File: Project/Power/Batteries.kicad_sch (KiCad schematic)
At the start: 12 parts, among them J1 Battery, J2 Battery, J3 Battery, J4 Battery, Q3 SQJ138ELP, Q4 SQJ138ELP, Q5 SQJ138ELP, Q6 SQJ138ELP, U3 NCV68061, U4 NCV68061, U5 NCV68061, U6 NCV68061

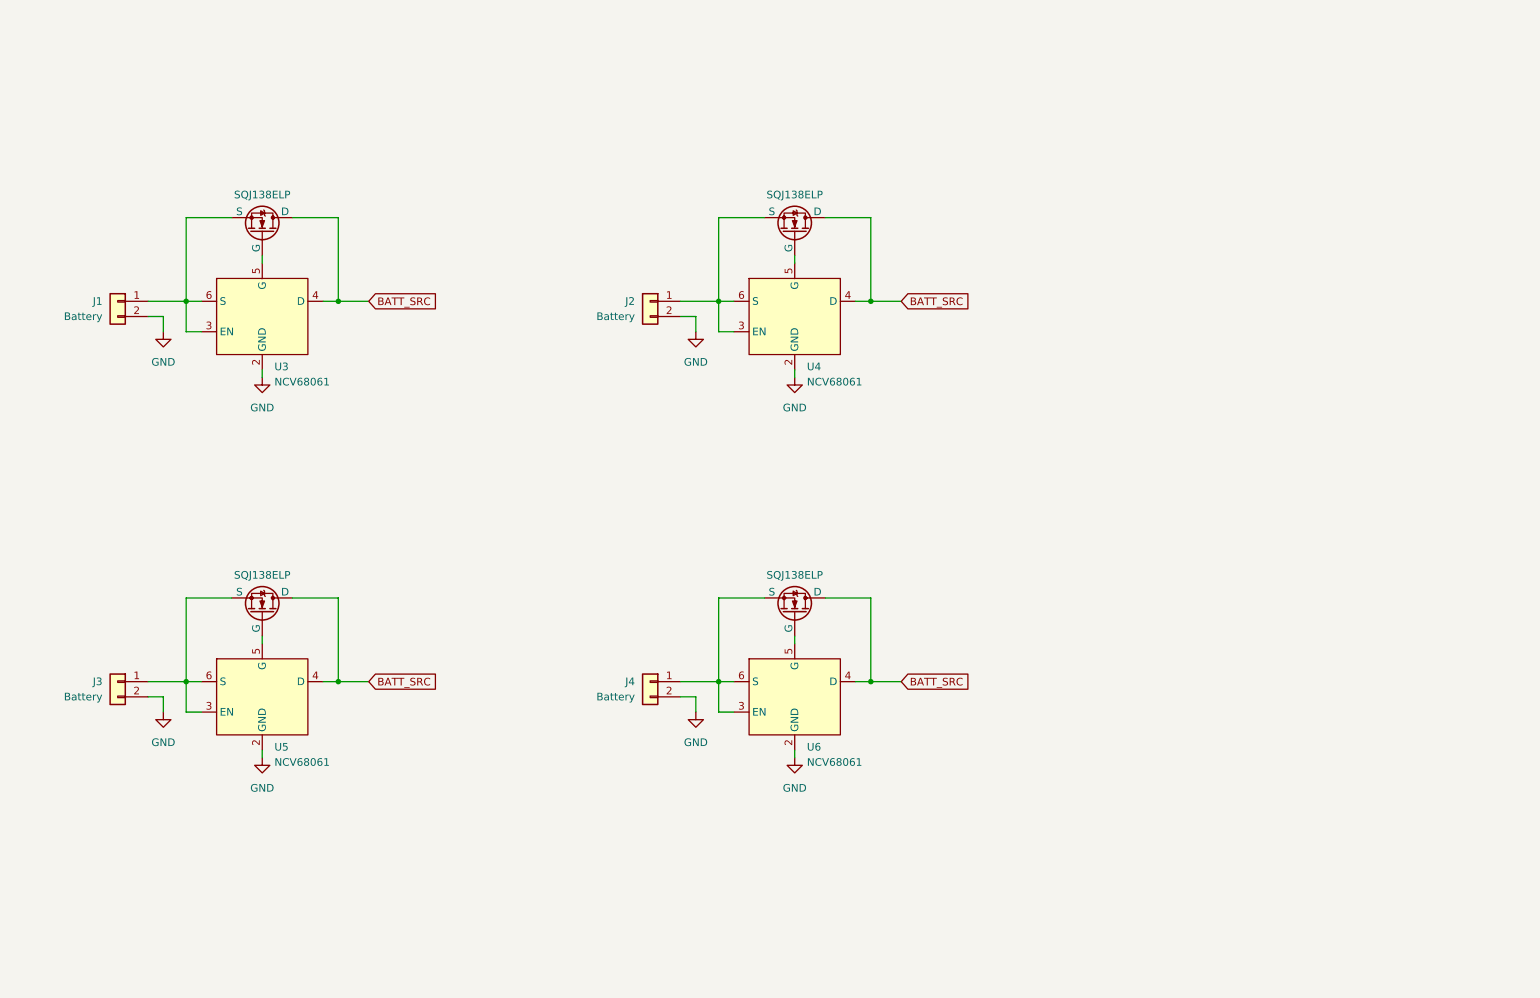
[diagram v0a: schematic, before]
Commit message: Add indicator LEDs to the batteries
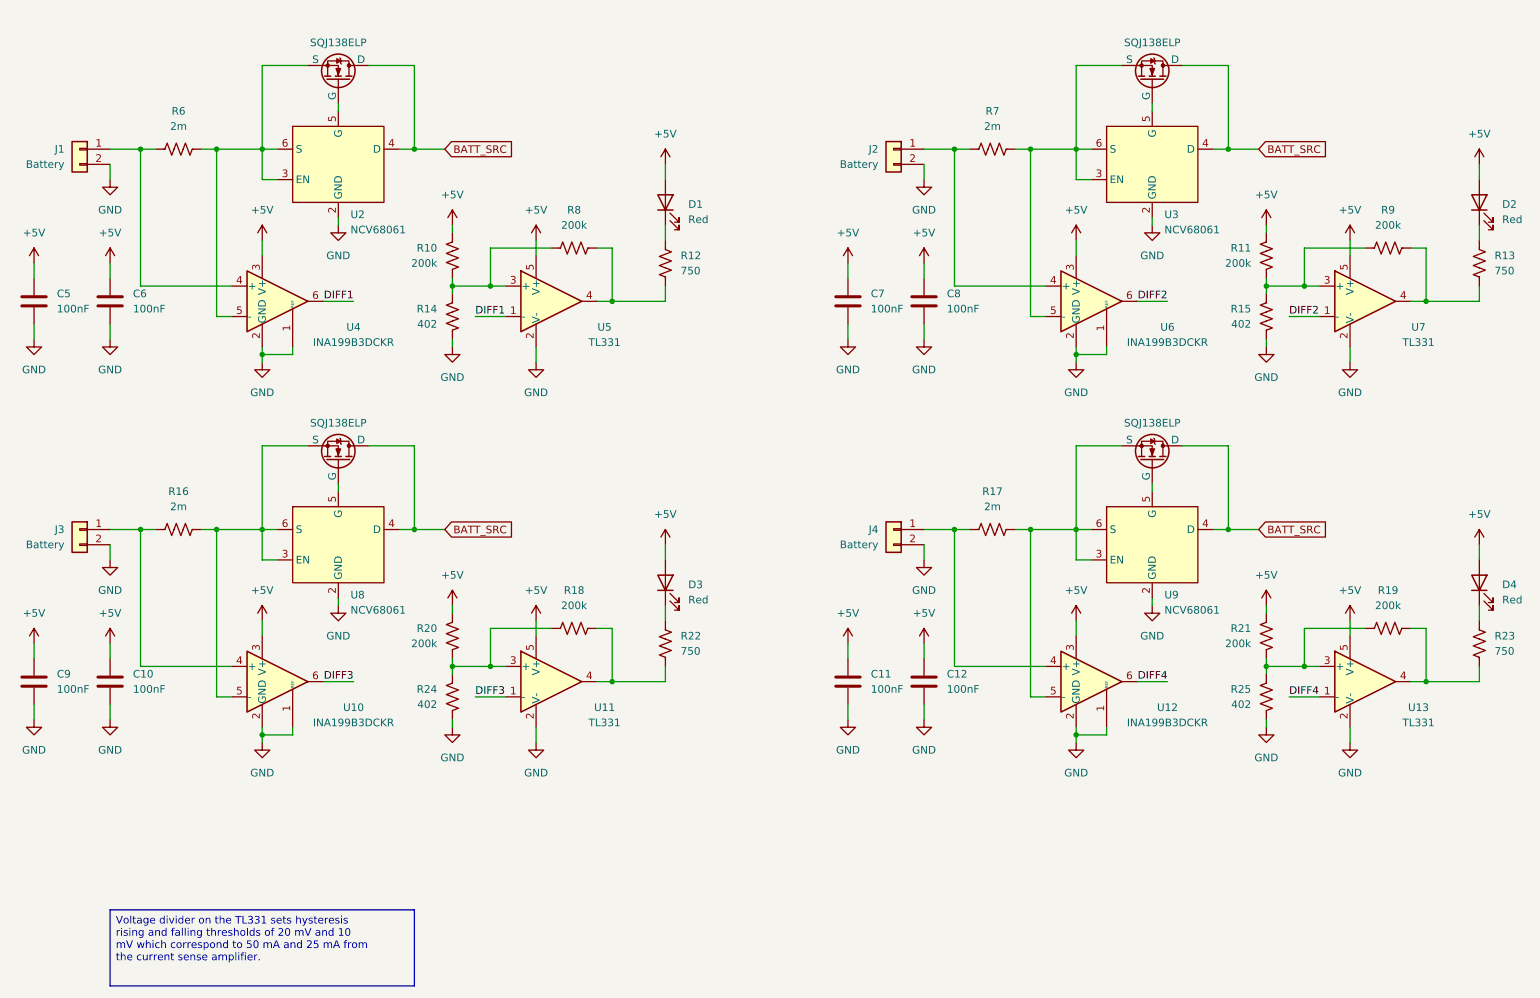
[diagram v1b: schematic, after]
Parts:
- removed U4, U5, U6: NCV68061, Package_TO_SOT_SMD:TSOT-23-6, symbol XuLab:NCV68061
- added C10, C11, C12, C5, C6, C7, C8, C9: 100nF, Capacitor_SMD:C_0603_1608Metric, symbol Device:C
- added D1, D2, D3, D4: Red, LED_SMD:LED_0603_1608Metric, symbol Device:LED
- added R10, R11, R18, R19, R20, R21, R8, R9: 200k, Resistor_SMD:R_0603_1608Metric, symbol Device:R_US
- added R12, R13, R22, R23: 750, Resistor_SMD:R_0603_1608Metric, symbol Device:R_US
- added R14, R15, R24, R25: 402, Resistor_SMD:R_0603_1608Metric, symbol Device:R_US
- added R16, R17, R6, R7: 2m, Resistor_SMD:R_2512_6332Metric, symbol Device:R_US
- added U10, U12, U4, U6: INA199B3DCKR, Package_TO_SOT_SMD:SOT-363_SC-70-6, symbol Amplifier_Current:INA199xxDCK
- added U11, U13, U5, U7: TL331, Package_TO_SOT_SMD:SOT-23-5, symbol Comparator:TL331
- added U3, U8, U9: NCV68061, Package_TO_SOT_SMD:TSOT-23-6, symbol XuLab:NCV68061
- renumbered U3 to U2
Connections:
- net BATT_SRC: now also U3.4 (D), U8.4 (D), U9.4 (D)
- net GND: now also C10.2, C11.2, C12.2, C5.2, C6.2, C7.2, C8.2, C9.2, R14.2, R15.2, R24.2, R25.2, U10.1 (REF), U10.2 (GND), U11.2 (V-), U12.1 (REF), U12.2 (GND), U13.2 (V-), U3.1, U3.2 (GND), U4.1 (REF), U4.2 (GND), U5.2 (V-), U6.1 (REF), U6.2 (GND), U7.2 (V-), U8.1, U8.2 (GND), U9.1, U9.2 (GND)
- net at Q5.1 (S), Q5.2 (S), Q5.3 (S): now also R16.2, U10.5 (-), U8.3 (EN), U8.6 (S); no longer J3.1 (Pin_1)
- net at Q4.1 (S), Q4.2 (S), Q4.3 (S): now also R7.2, U3.3 (EN), U3.6 (S), U6.5 (-); no longer J2.1 (Pin_1)
- net at Q4.4 (G): now also U3.5 (G)
- net at Q3.1 (S), Q3.2 (S), Q3.3 (S)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: now also R6.2, U4.5 (-); no longer J1.1 (Pin_1)
- net at Q6.1 (S), Q6.2 (S), Q6.3 (S): now also R17.2, U12.5 (-), U9.3 (EN), U9.6 (S); no longer J4.1 (Pin_1)
- net at Q6.4 (G): now also U9.5 (G)
- net at Q5.4 (G): now also U8.5 (G)
- new net: R11.2, R15.1, R9.1, U7.3 (+)
- new net: J4.1 (Pin_1), R17.1, U12.4 (+)
- new net: D4.1 (K), R23.2
- new net: R13.1, R9.2, U7.4
- new net: J2.1 (Pin_1), R7.1, U6.4 (+)
- new net: D2.1 (K), R13.2
- new net: R10.2, R14.1, R8.1, U5.3 (+)
- new net: R12.1, R8.2, U5.4
- new net: R18.2, R22.1, U11.4
- new net: D3.1 (K), R22.2
- new net: D1.1 (K), R12.2
- new net: R19.1, R21.2, R25.1, U13.3 (+)
- new net: R19.2, R23.1, U13.4
- new net: R18.1, R20.2, R24.1, U11.3 (+)
- new net: J3.1 (Pin_1), R16.1, U10.4 (+)
- new net: J1.1 (Pin_1), R6.1, U4.4 (+)
- new net +5V: C10.1, C11.1, C12.1, C5.1, C6.1, C7.1, C8.1, C9.1, D1.2 (A), D2.2 (A), D3.2 (A), D4.2 (A), R10.1, R11.1, R20.1, R21.1, U10.3 (V+), U11.5 (V+), U12.3 (V+), U13.5 (V+), U4.3 (V+), U5.5 (V+), U6.3 (V+), U7.5 (V+)
- new net DIFF1: U4.6, U5.1 (-)
- new net DIFF2: U6.6, U7.1 (-)
- new net DIFF3: U10.6, U11.1 (-)
- new net DIFF4: U12.6, U13.1 (-)
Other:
- moved on the sheet: J1, U2

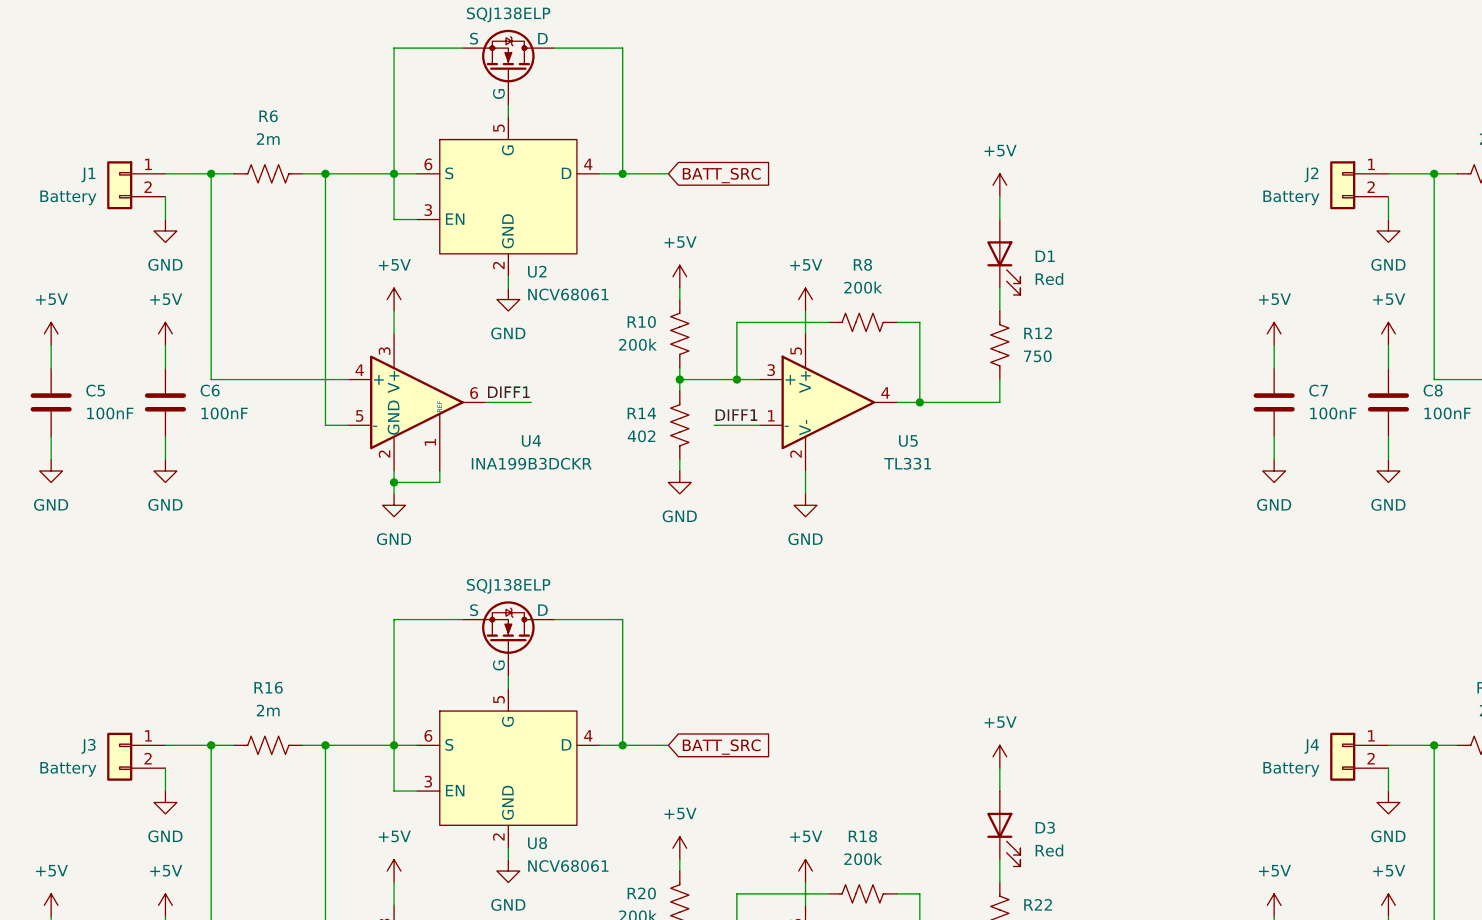
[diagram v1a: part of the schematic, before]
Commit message: Add servo connectors
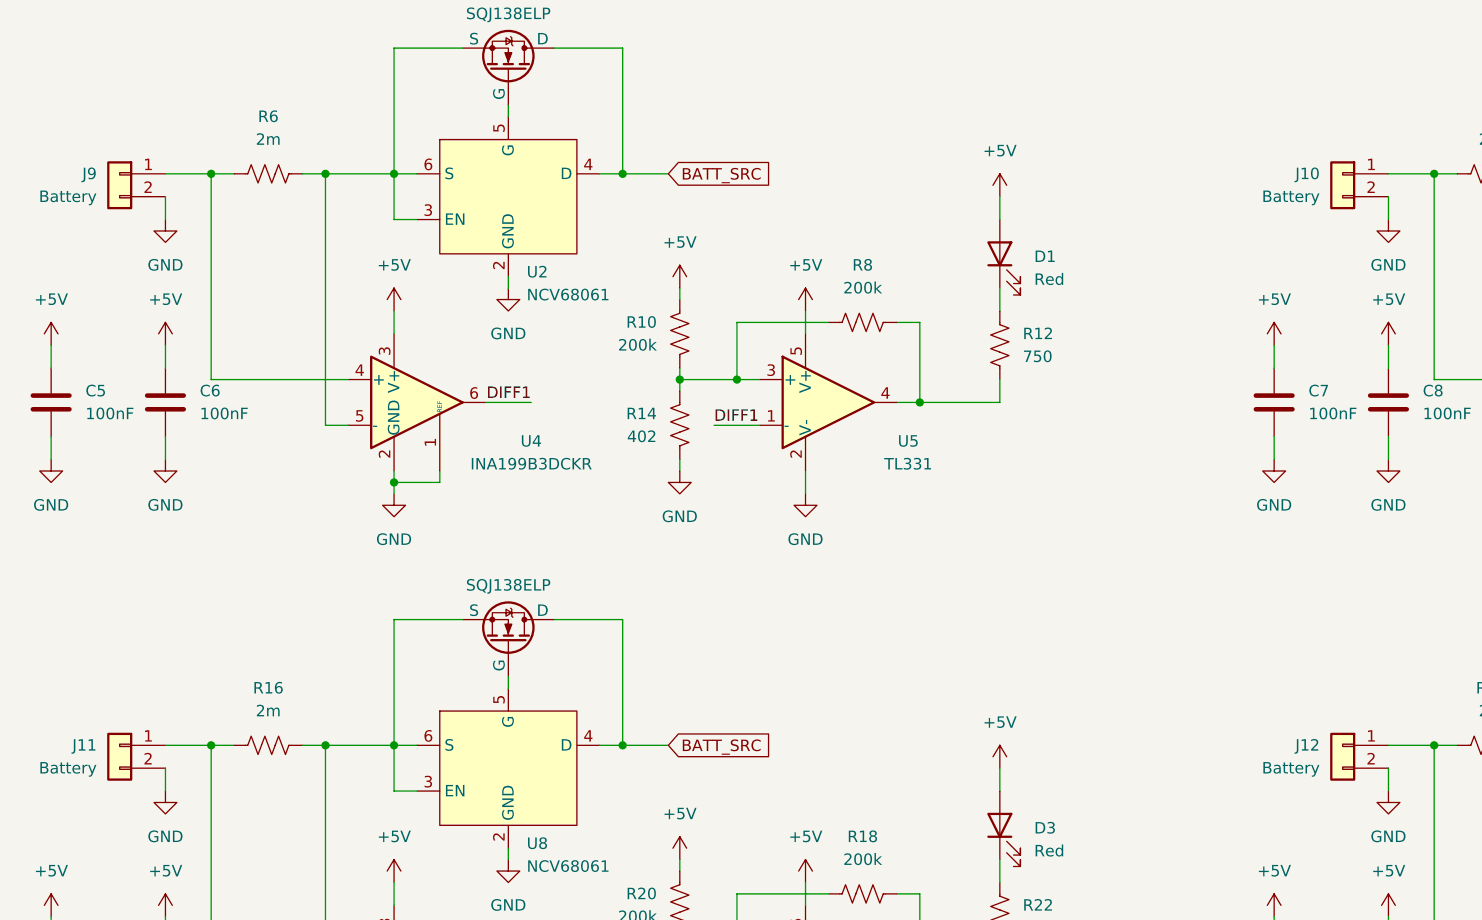
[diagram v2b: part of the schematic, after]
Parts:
- renumbered J2 to J10, J3 to J11, J4 to J12, J1 to J9
